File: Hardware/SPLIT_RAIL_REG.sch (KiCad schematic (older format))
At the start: 21 parts, among them Q14 PMOS, U18 TPS65130

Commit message: Currently adding level shifters
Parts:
- C70, C71, C72, C73, C74, C75, C76, C77, C78, C79: symbol C -> C-RESCUE-museV2
- R76, R77, R78, R79, R80: symbol R -> R-RESCUE-museV2
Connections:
- wire segments 91 -> 63
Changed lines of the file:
@@
 LIBS:microchip_pic18mcu
 LIBS:microchip
+LIBS:microchip1
 LIBS:microcontrollers
 LIBS:motorola
@@
 LIBS:sensors
 LIBS:siliconi
+LIBS:special
 LIBS:stm8
 LIBS:stm32
@@
 $EndComp
 $Comp
-L GND #PWR163
+L GND-RESCUE-museV2 #PWR163
 U 1 1 57DAC9F2
 P 5450 5000
@@
 $EndComp
 $Comp
-L C C73
+L C-RESCUE-museV2 C73
 U 1 1 57DACA1F
 P 6100 4750
@@
 $EndComp
 $Comp
-L C C74
+L C-RESCUE-museV2 C74
 U 1 1 57DACA4A
 P 6350 4750
@@
 $EndComp
 $Comp
-L GND #PWR164
+L GND-RESCUE-museV2 #PWR164
 U 1 1 57DACA83
 P 6100 5000
@@
 $EndComp
 $Comp
-L GND #PWR165
+L GND-RESCUE-museV2 #PWR165
 U 1 1 57DACA97
 P 6350 5000
@@
 $EndComp
 $Comp
-L GND #PWR166
+L GND-RESCUE-museV2 #PWR166
 U 1 1 57DACC08
 P 6600 5000
@@
 $EndComp
 $Comp
-L GND #PWR170
+L GND-RESCUE-museV2 #PWR170
 U 1 1 57DACD4E
 P 7550 5000
@@
 $EndComp
 Wire Wire Line
-	5450 4800 5450 4900
-Wire Wire Line
-	5450 4900 5450 5000
+	5450 4800 5450 5000
 Wire Wire Line
 	5350 4800 5350 4900
 Wire Wire Line
-	5350 4900 5450 4900
-Wire Wire Line
-	5450 4900 5550 4900
+	5350 4900 5550 4900
 Connection ~ 5450 4900
 Wire Wire Line
@@
 	6350 5000 6350 4900
 Wire Wire Line
-	6050 4200 6100 4200
-Wire Wire Line
-	6100 4200 6600 4200
-Wire Wire Line
-	6600 4200 6950 4200
+	6050 4200 6950 4200
 Wire Wire Line
 	6600 4200 6600 4650
@@
 	7150 4200 7550 4200
 Wire Wire Line
-	7550 4000 7550 4200
-Wire Wire Line
-	7550 4200 7550 4600
+	7550 4000 7550 4600
 Wire Wire Line
 	7550 5000 7550 4900
 Wire Wire Line
-	6050 4000 6300 4000
-Wire Wire Line
-	6300 4000 6500 4000
-Wire Wire Line
-	6500 4000 7550 4000
-Wire Wire Line
-	7550 4000 7850 4000
+	6050 4000 7850 4000
 Connection ~ 7550 4200
 Wire Wire Line
@@
 Connection ~ 6100 4200
 $Comp
-L R R78
+L R-RESCUE-museV2 R78
 U 1 1 57DACF39
 P 6300 3800
@@
 $EndComp
 $Comp
-L C C75
+L C-RESCUE-museV2 C75
 U 1 1 57DACF8B
 P 6500 3800
@@
 $EndComp
 $Comp
-L R R77
+L R-RESCUE-museV2 R77
 U 1 1 57DACFF1
 P 6300 3400
@@
 $EndComp
 Wire Wire Line
-	6050 3600 6300 3600
-Wire Wire Line
-	6300 3600 6500 3600
+	6050 3600 6500 3600
 Wire Wire Line
 	6500 3600 6500 3650
 Wire Wire Line
-	6300 3550 6300 3600
-Wire Wire Line
-	6300 3600 6300 3650
+	6300 3550 6300 3650
 Connection ~ 6300 3600
 Wire Wire Line
@@
 Connection ~ 6500 4000
 Wire Wire Line
-	6050 3200 6300 3200
-Wire Wire Line
-	6300 3200 6850 3200
+	6050 3200 6850 3200
 Wire Wire Line
 	6300 3200 6300 3250
 $Comp
-L C C76
+L C-RESCUE-museV2 C76
 U 1 1 57DADA01
 P 6850 3400
@@
 Connection ~ 6300 3200
 $Comp
-L GND #PWR167
+L GND-RESCUE-museV2 #PWR167
 U 1 1 57DADA89
 P 6850 3750
@@
 	6850 3550 6850 3750
 Wire Wire Line
-	4450 4500 4550 4500
-Wire Wire Line
-	4550 4500 4800 4500
-Wire Wire Line
-	4800 4500 4850 4500
-Wire Wire Line
-	4800 3700 4800 4200
-Wire Wire Line
-	4800 4200 4800 4300
-Wire Wire Line
-	4800 4300 4800 4400
-Wire Wire Line
-	4800 4400 4800 4500
+	4450 4500 4850 4500
+Wire Wire Line
+	4800 3700 4800 4500
 Wire Wire Line
 	4800 3700 4850 3700
@@
 Connection ~ 4800 4200
 $Comp
-L C C72
+L C-RESCUE-museV2 C72
 U 1 1 57DAE032
 P 4550 4750
@@
 Connection ~ 4800 4500
 $Comp
-L R R76
+L R-RESCUE-museV2 R76
 U 1 1 57DAE140
 P 4300 4500
@@
 $EndComp
 Wire Wire Line
-	4050 2550 4050 3600
-Wire Wire Line
-	4050 3600 4050 4500
-Wire Wire Line
-	4050 4500 4050 4600
+	4050 2550 4050 4600
 Connection ~ 4550 4500
 Wire Wire Line
 	4050 4500 4150 4500
 $Comp
-L GND #PWR162
+L GND-RESCUE-museV2 #PWR162
 U 1 1 57DAE30A
 P 4550 5000
@@
 	4550 5000 4550 4900
 $Comp
-L GND #PWR160
+L GND-RESCUE-museV2 #PWR160
 U 1 1 57DAE3B0
 P 4050 5000
@@
 	4050 5000 4050 4900
 Wire Wire Line
-	4050 3600 4800 3600
-Wire Wire Line
-	4800 3600 4850 3600
+	4050 3600 4850 3600
 Connection ~ 4050 4500
 Wire Wire Line
@@
 VIN
 Wire Wire Line
-	3600 2550 4050 2550
-Wire Wire Line
-	4050 2550 4100 2550
+	3600 2550 4100 2550
 Connection ~ 4050 3600
 $Comp
@@
 	4800 3100 4850 3100
 Wire Wire Line
-	4800 2550 4800 3000
-Wire Wire Line
-	4800 3000 4800 3100
+	4800 2550 4800 3100
 Wire Wire Line
 	4800 3000 4850 3000
 Connection ~ 4800 3000
 Wire Wire Line
-	4500 2550 4550 2550
-Wire Wire Line
-	4550 2550 4600 2550
+	4500 2550 4600 2550
 Wire Wire Line
 	4550 2550 4550 2700
 Connection ~ 4550 2550
 $Comp
-L C C71
+L C-RESCUE-museV2 C71
 U 1 1 57DAEAFC
 P 4550 2850
@@
 $EndComp
 $Comp
-L GND #PWR161
+L GND-RESCUE-museV2 #PWR161
 U 1 1 57DAEBCD
 P 4550 3050
@@
 Connection ~ 7550 4000
 Wire Wire Line
-	5550 2550 6100 2550
-Wire Wire Line
-	6100 2550 7050 2550
-Wire Wire Line
-	7050 2550 7250 2550
-Wire Wire Line
-	7250 2550 7550 2550
-Wire Wire Line
-	7550 2550 7850 2550
+	5550 2550 7850 2550
 Wire Wire Line
 	6050 3000 6100 3000
@@
 Connection ~ 6100 2550
 $Comp
-L R R80
+L R-RESCUE-museV2 R80
 U 1 1 57DAF2BE
 P 7250 3400
@@
 $EndComp
 $Comp
-L GND #PWR168
+L GND-RESCUE-museV2 #PWR168
 U 1 1 57DAF32E
 P 7250 3750
@@
 	7250 3550 7250 3750
 Wire Wire Line
-	6050 3100 7050 3100
-Wire Wire Line
-	7050 3100 7250 3100
-Wire Wire Line
-	7250 3000 7250 3100
-Wire Wire Line
-	7250 3100 7250 3250
-$Comp
-L R R79
+	6050 3100 7250 3100
+Wire Wire Line
+	7250 3000 7250 3250
+$Comp
+L R-RESCUE-museV2 R79
 U 1 1 57DAF532
 P 7050 2850
@@
 Connection ~ 7250 2550
 $Comp
-L C C77
+L C-RESCUE-museV2 C77
 U 1 1 57DAF6D3
 P 7250 2850
@@
 $EndComp
 $Comp
-L C C78
+L C-RESCUE-museV2 C78
 U 1 1 57DAF88B
 P 7550 2850
@@
 Connection ~ 7550 2550
 $Comp
-L GND #PWR169
+L GND-RESCUE-museV2 #PWR169
 U 1 1 57DAF96B
 P 7550 3750
@@
 	7550 3750 7550 3000
 $Comp
-L C C70
+L C-RESCUE-museV2 C70
 U 1 1 57DB07FA
 P 4050 4750
@@
 $EndComp
 $Comp
-L C C79
+L C-RESCUE-museV2 C79
 U 1 1 57DB11B4
 P 7550 4750

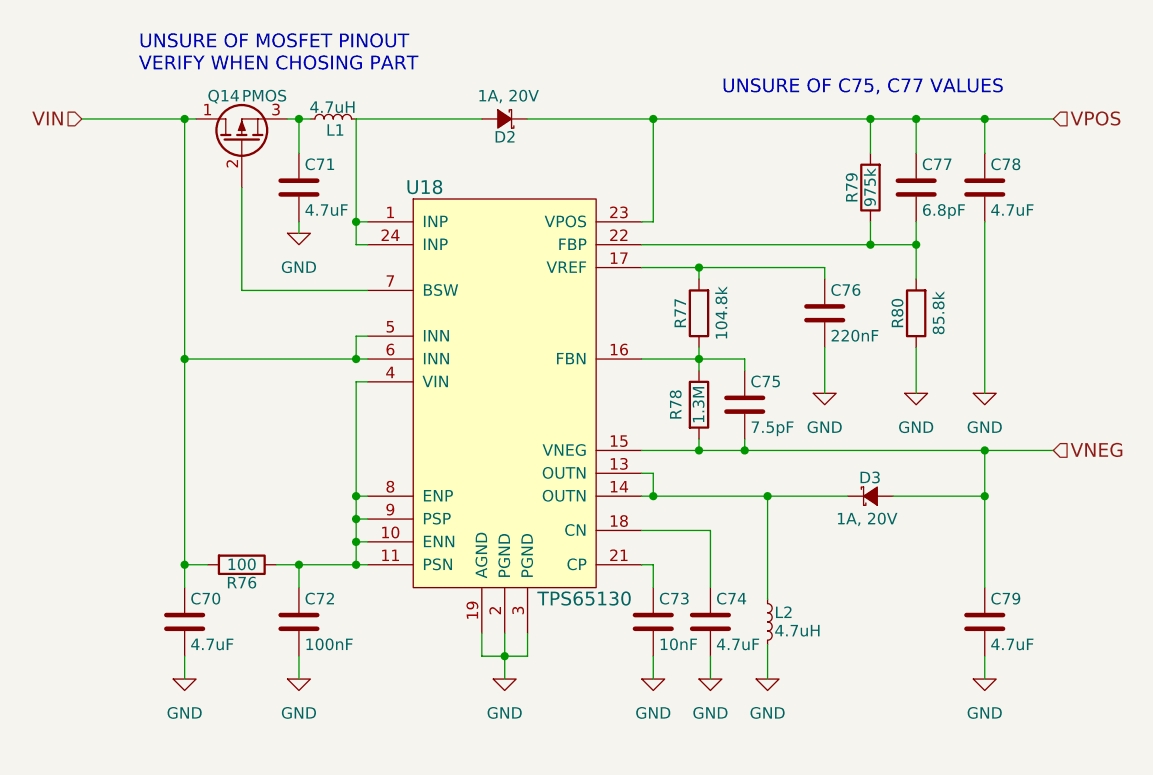
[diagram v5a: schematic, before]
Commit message: Changing to global labels/pages in progress
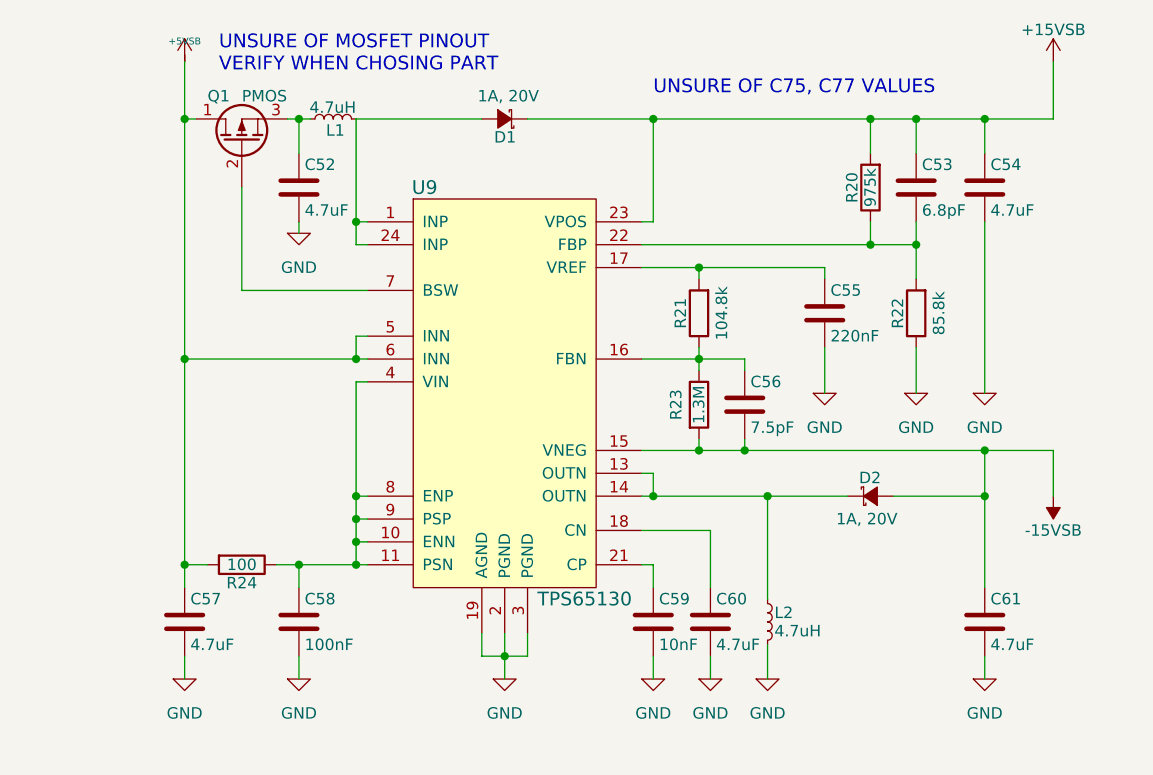
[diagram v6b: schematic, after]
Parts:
- renumbered C71 to C52, C77 to C53, C78 to C54, C76 to C55, C75 to C56, C70 to C57, C72 to C58, C73 to C59, C74 to C60, C79 to C61, D2 to D1, D3 to D2, Q14 to Q1, R79 to R20, R77 to R21, R80 to R22, R78 to R23, R76 to R24, U18 to U9
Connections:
- net VIN renamed +5VSB
- net VNEG renamed -15V
- net VPOS renamed +15V

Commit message: Finished converting to global labels
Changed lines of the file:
@@
 $Descr A4 11693 8268
 encoding utf-8
-Sheet 4 8
+Sheet 2 10
 Title ""
 Date ""
@@
 $EndComp
 Wire Wire Line
-	5450 4800 5450 4900
-Wire Wire Line
-	5450 4900 5450 5000
+	5450 4800 5450 5000
 Wire Wire Line
 	5350 4800 5350 4900
 Wire Wire Line
-	5350 4900 5450 4900
-Wire Wire Line
-	5450 4900 5550 4900
+	5350 4900 5550 4900
 Connection ~ 5450 4900
 Wire Wire Line
@@
 	6350 5000 6350 4900
 Wire Wire Line
-	6050 4200 6100 4200
-Wire Wire Line
-	6100 4200 6600 4200
-Wire Wire Line
-	6600 4200 6950 4200
+	6050 4200 6950 4200
 Wire Wire Line
 	6600 4200 6600 4650
@@
 	7150 4200 7550 4200
 Wire Wire Line
-	7550 4000 7550 4200
-Wire Wire Line
-	7550 4200 7550 4600
+	7550 4000 7550 4600
 Wire Wire Line
 	7550 5000 7550 4900
 Wire Wire Line
-	6050 4000 6300 4000
-Wire Wire Line
-	6300 4000 6500 4000
-Wire Wire Line
-	6500 4000 7550 4000
-Wire Wire Line
-	7550 4000 7850 4000
+	6050 4000 7850 4000
 Connection ~ 7550 4200
 Wire Wire Line
@@
 $EndComp
 Wire Wire Line
-	6050 3600 6300 3600
-Wire Wire Line
-	6300 3600 6500 3600
+	6050 3600 6500 3600
 Wire Wire Line
 	6500 3600 6500 3650
 Wire Wire Line
-	6300 3550 6300 3600
-Wire Wire Line
-	6300 3600 6300 3650
+	6300 3550 6300 3650
 Connection ~ 6300 3600
 Wire Wire Line
@@
 Connection ~ 6500 4000
 Wire Wire Line
-	6050 3200 6300 3200
-Wire Wire Line
-	6300 3200 6850 3200
+	6050 3200 6850 3200
 Wire Wire Line
 	6300 3200 6300 3250
@@
 	6850 3550 6850 3750
 Wire Wire Line
-	4450 4500 4550 4500
-Wire Wire Line
-	4550 4500 4800 4500
-Wire Wire Line
-	4800 4500 4850 4500
-Wire Wire Line
-	4800 3700 4800 4200
-Wire Wire Line
-	4800 4200 4800 4300
-Wire Wire Line
-	4800 4300 4800 4400
-Wire Wire Line
-	4800 4400 4800 4500
+	4450 4500 4850 4500
+Wire Wire Line
+	4800 3700 4800 4500
 Wire Wire Line
 	4800 3700 4850 3700
@@
 $EndComp
 Wire Wire Line
-	4050 2300 4050 2550
-Wire Wire Line
-	4050 2550 4050 3600
-Wire Wire Line
-	4050 3600 4050 4500
-Wire Wire Line
-	4050 4500 4050 4600
+	4050 2300 4050 4600
 Connection ~ 4550 4500
 Wire Wire Line
@@
 	4050 5000 4050 4900
 Wire Wire Line
-	4050 3600 4800 3600
-Wire Wire Line
-	4800 3600 4850 3600
+	4050 3600 4850 3600
 Connection ~ 4050 4500
 Wire Wire Line
@@
 	4800 3100 4850 3100
 Wire Wire Line
-	4800 2550 4800 3000
-Wire Wire Line
-	4800 3000 4800 3100
+	4800 2550 4800 3100
 Wire Wire Line
 	4800 3000 4850 3000
 Connection ~ 4800 3000
 Wire Wire Line
-	4500 2550 4550 2550
-Wire Wire Line
-	4550 2550 4600 2550
+	4500 2550 4600 2550
 Wire Wire Line
 	4550 2550 4550 2700
@@
 	7250 3550 7250 3750
 Wire Wire Line
-	6050 3100 7050 3100
-Wire Wire Line
-	7050 3100 7250 3100
-Wire Wire Line
-	7250 3000 7250 3100
-Wire Wire Line
-	7250 3100 7250 3250
+	6050 3100 7250 3100
+Wire Wire Line
+	7250 3000 7250 3250
 $Comp
 L R-RESCUE-museV2 R20
@@
 	4100 2550 4050 2550
 Wire Wire Line
-	5550 2550 6100 2550
-Wire Wire Line
-	6100 2550 7050 2550
-Wire Wire Line
-	7050 2550 7250 2550
-Wire Wire Line
-	7250 2550 7550 2550
-Wire Wire Line
-	7550 2550 7850 2550
+	5550 2550 7850 2550
 $Comp
 L -15VSB #PWR?
